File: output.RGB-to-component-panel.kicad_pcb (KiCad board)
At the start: 2 copper layers, 105 x 145 mm, 256 parts, among them J1 VGA, J3 USB_C_Receptacle_Power, J4 SCART_CONN, J5 3xRCA_CONN, U1 SC6206B-65K5, U101 TPF144-VR, U2 TPF144-VR, U3 RS8752XM, U6 74AHCT1G86, U7 74AHCT1G86, U8 LM1881

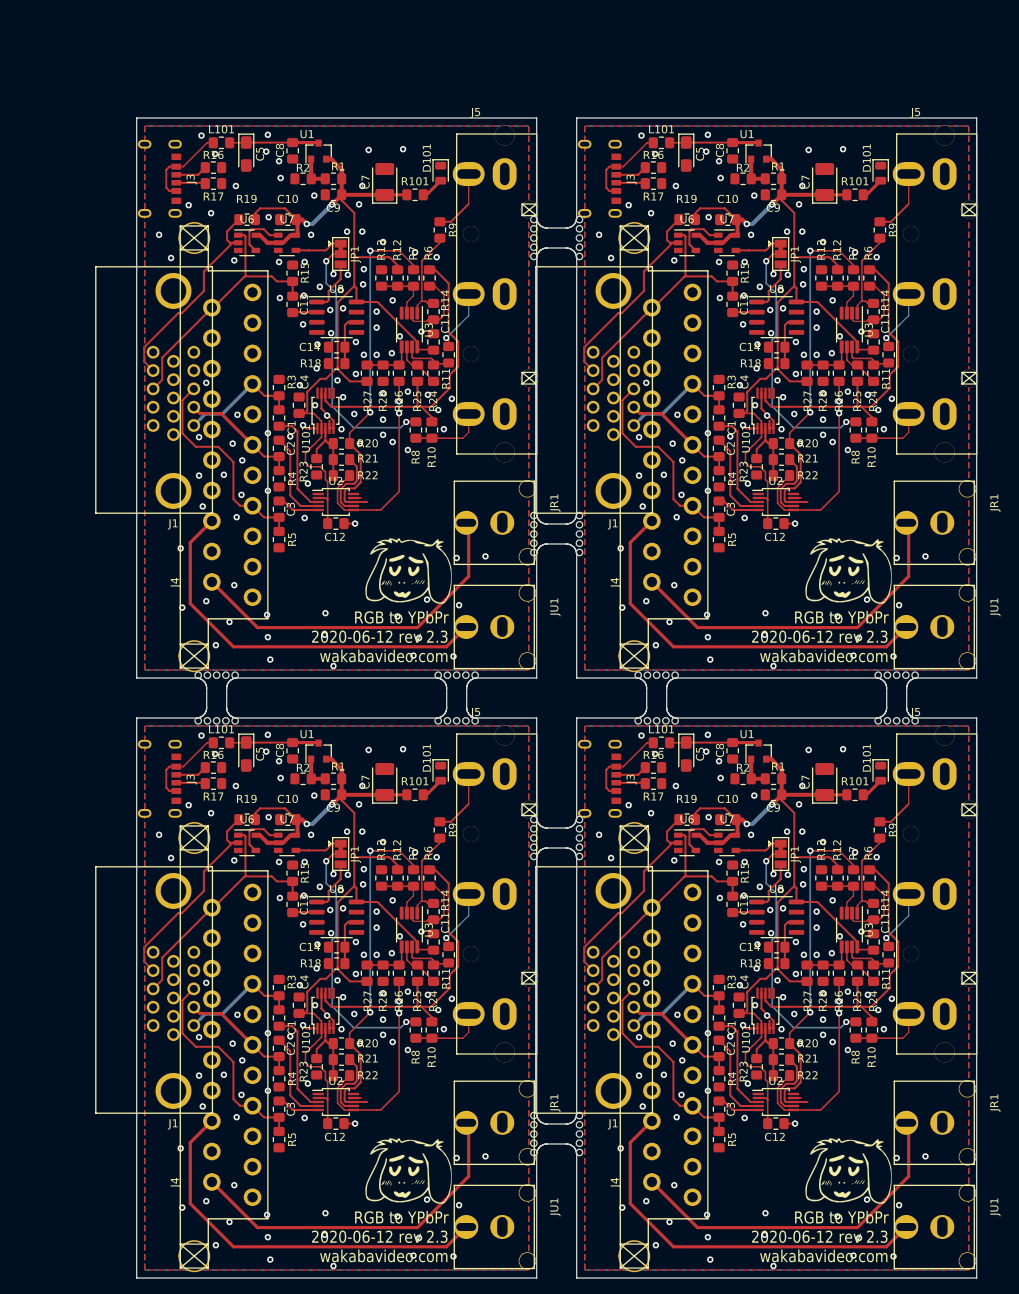
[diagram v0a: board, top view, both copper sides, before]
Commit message: swapped opamp for SOIC package
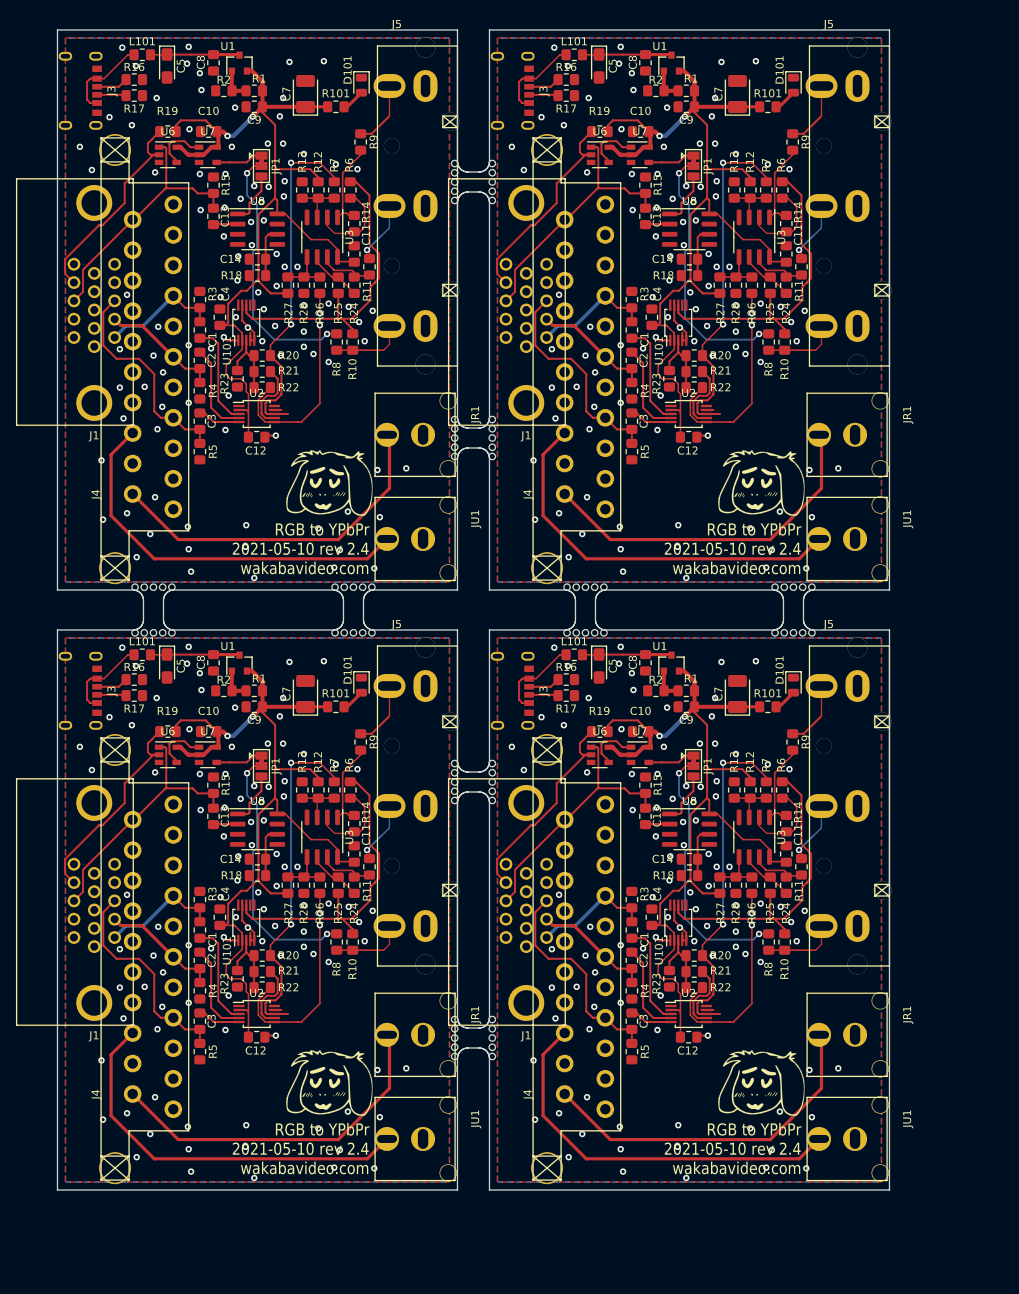
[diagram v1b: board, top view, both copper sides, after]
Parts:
- removed the ? at (79.5, 180.3)
- removed the ? at (122.5, 120.7)
- removed the ? at (97.1, 126.3)
- removed the ? at (92.5, 120.7)
- removed the ? at (67.5, 120.7)
- removed the ? at (72.1, 126.3)
- removed the ? at (37.5, 120.7)
- removed the ? at (42.1, 126.3)
- removed the ? at (85.2, 175.7)
- removed the ? at (79.5, 143.3)
- removed the ? at (85.2, 138.7)
- removed the ? at (79.5, 105.3)
- removed the ? at (85.2, 100.7)
- removed the ? at (79.5, 68.3)
- removed the ? at (85.2, 63.7)
- removed the ? at (127.1, 126.3)
- removed the C1 at (102.6, 163.5)
- removed the C1 at (47.6, 163.5)
- removed the C1 at (47.6, 88.5)
- removed the C1 at (102.6, 88.5)
- removed the C10 at (103.7, 138.7)
- removed the C10 at (48.7, 138.7)
- removed the C10 at (48.7, 63.7)
- removed the C10 at (103.7, 63.7)
- removed the C11 at (121.9, 154.0)
- removed the C11 at (66.9, 154.0)
- removed the C11 at (66.9, 79.0)
- removed the C11 at (121.9, 79.0)
- removed the C12 at (109.7, 176.7)
- removed the C12 at (54.7, 176.7)
- removed the C12 at (54.7, 101.7)
- removed the C12 at (109.7, 101.7)
- removed the C13 at (104.3, 149.3)
- removed the C13 at (49.3, 149.3)
- removed the C13 at (49.3, 74.3)
- removed the C13 at (104.3, 74.3)
- removed the C14 at (109.8, 154.7)
- removed the C14 at (54.8, 154.7)
- removed the C14 at (54.8, 79.7)
- removed the C14 at (109.8, 79.7)
- removed the C2 at (102.6, 167.3)
- removed the C2 at (47.6, 167.3)
- removed the C2 at (47.6, 92.3)
- removed the C2 at (102.6, 92.3)
- removed the C3 at (102.6, 174.9)
- removed the C3 at (47.6, 174.9)
- removed the C3 at (47.6, 99.9)
- removed the C3 at (102.6, 99.9)
- removed the C4 at (105.1, 161.9)
- removed the C4 at (50.1, 161.9)
- removed the C4 at (50.1, 86.9)
- removed the C4 at (105.1, 86.9)
- removed the C5 at (98.5, 130.5)
- removed the C5 at (43.5, 130.5)
- removed the C5 at (43.5, 55.5)
- removed the C5 at (98.5, 55.5)
- removed the C7 at (115.8, 134.0)
- removed the C7 at (60.8, 134.0)
- removed the C7 at (60.8, 59.0)
- removed the C7 at (115.8, 59.0)
- removed the C8 at (104.3, 130.1)
- removed the C8 at (49.3, 130.1)
- removed the C8 at (49.3, 55.1)
- removed the C8 at (104.3, 55.1)
- removed the C9 at (109.4, 135.6)
- removed the C9 at (54.4, 135.6)
- removed the C9 at (54.4, 60.6)
- removed the C9 at (109.4, 60.6)
- removed the D101 at (122.8, 132.9)
- removed the D101 at (67.8, 132.9)
- removed the D101 at (67.8, 57.9)
- removed the D101 at (122.8, 57.9)
- removed the GOTE1 at (118.8, 182.6)
- removed the GOTE1 at (63.8, 182.6)
- removed the GOTE1 at (63.8, 107.6)
- removed the GOTE1 at (118.8, 107.6)
- removed the GOTE2 at (112.6, 166.7)
- removed the GOTE2 at (57.6, 166.7)
- removed the GOTE2 at (57.6, 91.7)
- removed the GOTE2 at (112.6, 91.7)
- removed the J1 at (89.4, 161.0)
- removed the J1 at (34.4, 161.0)
- removed the J1 at (34.4, 86.0)
- removed the J1 at (89.4, 86.0)
- removed the J3 at (83.2, 133.6)
- removed the J3 at (28.2, 133.6)
- removed the J3 at (28.2, 58.6)
- removed the J3 at (83.2, 58.6)
- removed the J4 at (94.2, 184.0)
- removed the J4 at (39.2, 184.0)
- removed the J4 at (39.2, 109.0)
- removed the J4 at (94.2, 109.0)
- removed the J5 at (130.8, 148.0)
- removed the J5 at (75.8, 148.0)
- removed the J5 at (75.8, 73.0)
- removed the J5 at (130.8, 73.0)
- removed the JP1 at (110.3, 143.0)
- removed the JP1 at (55.3, 143.0)
- removed the JP1 at (55.3, 68.0)
- removed the JP1 at (110.3, 68.0)
- removed the JR1 at (134.5, 176.6)
- removed the JR1 at (79.5, 176.6)
- removed the JR1 at (79.5, 101.6)
- removed the JR1 at (134.5, 101.6)
- removed the JU1 at (134.5, 189.6)
- removed the JU1 at (79.5, 189.6)
- removed the JU1 at (79.5, 114.6)
- removed the JU1 at (134.5, 114.6)
- removed the L101 at (95.4, 129.1)
- removed the L101 at (40.4, 129.1)
- removed the L101 at (40.4, 54.1)
- removed the L101 at (95.4, 54.1)
- removed the R1 at (109.4, 133.6)
- removed the R1 at (54.4, 133.6)
- removed the R1 at (54.4, 58.6)
- removed the R1 at (109.4, 58.6)
- removed the R10 at (121.7, 165.0)
- removed the R10 at (66.7, 165.0)
- removed the R10 at (66.7, 90.0)
- removed the R10 at (121.7, 90.0)
- removed the R101 at (119.6, 135.6)
- removed the R101 at (64.6, 135.6)
- removed the R101 at (64.6, 60.6)
- removed the R101 at (119.6, 60.6)
- removed the R11 at (123.8, 155.6)
- removed the R11 at (68.8, 155.6)
- removed the R11 at (68.8, 80.6)
- removed the R11 at (123.8, 80.6)
- removed the R12 at (117.4, 146.0)
- removed the R12 at (62.4, 146.0)
- removed the R12 at (62.4, 71.0)
- removed the R12 at (117.4, 71.0)
- removed the R13 at (115.4, 146.0)
- removed the R13 at (60.4, 146.0)
- removed the R13 at (60.4, 71.0)
- removed the R13 at (115.4, 71.0)
- removed the R14 at (121.9, 150.2)
- removed the R14 at (66.9, 150.2)
- removed the R14 at (66.9, 75.2)
- removed the R14 at (121.9, 75.2)
- removed the R15 at (104.3, 145.4)
- removed the R15 at (49.3, 145.4)
- removed the R15 at (49.3, 70.4)
- removed the R15 at (104.3, 70.4)
- removed the R16 at (94.4, 132.2)
- removed the R16 at (39.4, 132.2)
- removed the R16 at (39.4, 57.2)
- removed the R16 at (94.4, 57.2)
- removed the R17 at (94.4, 134.2)
- removed the R17 at (39.4, 134.2)
- removed the R17 at (39.4, 59.2)
- removed the R17 at (94.4, 59.2)
- removed the R18 at (109.8, 156.7)
- removed the R18 at (54.8, 156.7)
- removed the R18 at (54.8, 81.7)
- removed the R18 at (109.8, 81.7)
- removed the R19 at (98.6, 138.7)
- removed the R19 at (43.6, 138.7)
- removed the R19 at (43.6, 63.7)
- removed the R19 at (98.6, 63.7)
- removed the R2 at (105.6, 133.6)
- removed the R2 at (50.6, 133.6)
- removed the R2 at (50.6, 58.6)
- removed the R2 at (105.6, 58.6)
- removed the R20 at (110.4, 166.7)
- removed the R20 at (55.4, 166.7)
- removed the R20 at (55.4, 91.7)
- removed the R20 at (110.4, 91.7)
- removed the R21 at (110.4, 168.7)
- removed the R21 at (55.4, 168.7)
- removed the R21 at (55.4, 93.7)
- removed the R21 at (110.4, 93.7)
- removed the R22 at (110.4, 170.7)
- removed the R22 at (55.4, 170.7)
- removed the R22 at (55.4, 95.7)
- removed the R22 at (110.4, 95.7)
- removed the R23 at (107.3, 169.6)
- removed the R23 at (52.3, 169.6)
- removed the R23 at (52.3, 94.6)
- removed the R23 at (107.3, 94.6)
- removed the R24 at (121.9, 157.9)
- removed the R24 at (66.9, 157.9)
- removed the R24 at (66.9, 82.9)
- removed the R24 at (121.9, 82.9)
- removed the R25 at (119.9, 157.9)
- removed the R25 at (64.9, 157.9)
- removed the R25 at (64.9, 82.9)
- removed the R25 at (119.9, 82.9)
- removed the R26 at (117.6, 157.9)
- removed the R26 at (62.6, 157.9)
- removed the R26 at (62.6, 82.9)
- removed the R26 at (117.6, 82.9)
- removed the R27 at (113.6, 157.9)
- removed the R27 at (58.6, 157.9)
- removed the R27 at (58.6, 82.9)
- removed the R27 at (113.6, 82.9)
- removed the R28 at (115.6, 157.9)
- removed the R28 at (60.6, 157.9)
- removed the R28 at (60.6, 82.9)
- removed the R28 at (115.6, 82.9)
- removed the R3 at (102.6, 159.7)
- removed the R3 at (47.6, 159.7)
- removed the R3 at (47.6, 84.7)
- removed the R3 at (102.6, 84.7)
- removed the R4 at (102.6, 171.1)
- removed the R4 at (47.6, 171.1)
- removed the R4 at (47.6, 96.1)
- removed the R4 at (102.6, 96.1)
- removed the R5 at (102.6, 178.7)
- removed the R5 at (47.6, 178.7)
- removed the R5 at (47.6, 103.7)
- removed the R5 at (102.6, 103.7)
- removed the R6 at (121.4, 146.0)
- removed the R6 at (66.4, 146.0)
- removed the R6 at (66.4, 71.0)
- removed the R6 at (121.4, 71.0)
- removed the R7 at (119.4, 146.0)
- removed the R7 at (64.4, 146.0)
- removed the R7 at (64.4, 71.0)
- removed the R7 at (119.4, 71.0)
- removed the R8 at (119.7, 165.0)
- removed the R8 at (64.7, 165.0)
- removed the R8 at (64.7, 90.0)
- removed the R8 at (119.7, 90.0)
- removed the R9 at (122.7, 140.0)
- removed the R9 at (67.7, 140.0)
- removed the R9 at (67.7, 65.0)
- removed the R9 at (122.7, 65.0)
- removed the U1 at (107.5, 130.1)
- removed the U1 at (52.5, 130.1)
- removed the U1 at (52.5, 55.1)
- removed the U1 at (107.5, 55.1)
- removed the U101 at (108.4, 162.6)
- removed the U101 at (53.4, 162.6)
- removed the U101 at (53.4, 87.6)
- removed the U101 at (108.4, 87.6)
- removed the U2 at (109.7, 174.0)
- removed the U2 at (54.7, 174.0)
- removed the U2 at (54.7, 99.0)
- removed the U2 at (109.7, 99.0)
- removed the U3 at (118.9, 152.5)
- removed the U3 at (63.9, 152.5)
- removed the U3 at (63.9, 77.5)
- removed the U3 at (118.9, 77.5)
- removed the U6 at (98.6, 141.6)
- removed the U6 at (43.6, 141.6)
- removed the U6 at (43.6, 66.6)
- removed the U6 at (98.6, 66.6)
- removed the U7 at (103.6, 141.6)
- removed the U7 at (48.6, 141.6)
- removed the U7 at (48.6, 66.6)
- removed the U7 at (103.6, 66.6)
- removed the U8 at (109.8, 150.9)
- removed the U8 at (54.8, 150.9)
- removed the U8 at (54.8, 75.9)
- removed the U8 at (109.8, 75.9)
- added ?: , holes, F.Cu at (109.6, 109.6)
- added ?: , holes, F.Cu at (74.2, 131.7)
- added ?: , holes, F.Cu at (69.5, 168.3)
- added ?: , holes, F.Cu at (74.2, 163.7)
- added ?: , holes, F.Cu at (69.6, 61.3)
- added ?: , holes, F.Cu at (74.2, 56.7)
- added ?: , holes, F.Cu at (69.5, 93.3)
- added ?: , holes, F.Cu at (74.2, 88.7)
- added ?: , holes, F.Cu at (114.2, 115.4)
- added ?: , holes, F.Cu at (83.6, 109.7)
- added ?: , holes, F.Cu at (88.2, 115.3)
- added ?: , holes, F.Cu at (54.6, 109.7)
- added ?: , holes, F.Cu at (59.2, 115.3)
- added ?: , holes, F.Cu at (29.6, 109.7)
- added ?: , holes, F.Cu at (34.2, 115.3)
- added ?: , holes, F.Cu at (69.6, 136.3)
- added C1: 1u, Capacitor_SMD:C_0805_2012Metric_Pad1.15x1.40mm_HandSolder, F.Cu at (37.7, 152.5)
- added C1: 1u, Capacitor_SMD:C_0805_2012Metric_Pad1.15x1.40mm_HandSolder, F.Cu at (91.7, 152.5)
- added C1: 1u, Capacitor_SMD:C_0805_2012Metric_Pad1.15x1.40mm_HandSolder, F.Cu at (91.7, 77.5)
- added C1: 1u, Capacitor_SMD:C_0805_2012Metric_Pad1.15x1.40mm_HandSolder, F.Cu at (37.7, 77.5)
- added C10: 100n, Capacitor_SMD:C_0805_2012Metric_Pad1.15x1.40mm_HandSolder, F.Cu at (92.8, 127.7)
- added C10: 100n, Capacitor_SMD:C_0805_2012Metric_Pad1.15x1.40mm_HandSolder, F.Cu at (38.8, 127.7)
- added C10: 100n, Capacitor_SMD:C_0805_2012Metric_Pad1.15x1.40mm_HandSolder, F.Cu at (92.8, 52.7)
- added C10: 100n, Capacitor_SMD:C_0805_2012Metric_Pad1.15x1.40mm_HandSolder, F.Cu at (38.8, 52.7)
- added C11: 100n, Capacitor_SMD:C_0805_2012Metric_Pad1.15x1.40mm_HandSolder, F.Cu at (111.0, 143.0)
- added C11: 100n, Capacitor_SMD:C_0805_2012Metric_Pad1.15x1.40mm_HandSolder, F.Cu at (57.0, 143.0)
- added C11: 100n, Capacitor_SMD:C_0805_2012Metric_Pad1.15x1.40mm_HandSolder, F.Cu at (111.0, 68.0)
- added C11: 100n, Capacitor_SMD:C_0805_2012Metric_Pad1.15x1.40mm_HandSolder, F.Cu at (57.0, 68.0)
- added C12: 100n, Capacitor_SMD:C_0805_2012Metric_Pad1.15x1.40mm_HandSolder, F.Cu at (44.8, 165.9)
- added C12: 100n, Capacitor_SMD:C_0805_2012Metric_Pad1.15x1.40mm_HandSolder, F.Cu at (98.8, 165.9)
- added C12: 100n, Capacitor_SMD:C_0805_2012Metric_Pad1.15x1.40mm_HandSolder, F.Cu at (98.8, 90.9)
- added C12: 100n, Capacitor_SMD:C_0805_2012Metric_Pad1.15x1.40mm_HandSolder, F.Cu at (44.8, 90.9)
- added C13: 100n, Capacitor_SMD:C_0805_2012Metric_Pad1.15x1.40mm_HandSolder, F.Cu at (93.4, 138.3)
- added C13: 100n, Capacitor_SMD:C_0805_2012Metric_Pad1.15x1.40mm_HandSolder, F.Cu at (39.4, 138.3)
- added C13: 100n, Capacitor_SMD:C_0805_2012Metric_Pad1.15x1.40mm_HandSolder, F.Cu at (93.4, 63.3)
- added C13: 100n, Capacitor_SMD:C_0805_2012Metric_Pad1.15x1.40mm_HandSolder, F.Cu at (39.4, 63.3)
- added C14: 100n, Capacitor_SMD:C_0805_2012Metric_Pad1.15x1.40mm_HandSolder, F.Cu at (98.9, 143.7)
- added C14: 100n, Capacitor_SMD:C_0805_2012Metric_Pad1.15x1.40mm_HandSolder, F.Cu at (44.9, 143.7)
- added C14: 100n, Capacitor_SMD:C_0805_2012Metric_Pad1.15x1.40mm_HandSolder, F.Cu at (98.9, 68.7)
- added C14: 100n, Capacitor_SMD:C_0805_2012Metric_Pad1.15x1.40mm_HandSolder, F.Cu at (44.9, 68.7)
- added C2: 1u, Capacitor_SMD:C_0805_2012Metric_Pad1.15x1.40mm_HandSolder, F.Cu at (37.7, 156.3)
- added C2: 1u, Capacitor_SMD:C_0805_2012Metric_Pad1.15x1.40mm_HandSolder, F.Cu at (91.7, 156.3)
- added C2: 1u, Capacitor_SMD:C_0805_2012Metric_Pad1.15x1.40mm_HandSolder, F.Cu at (91.7, 81.3)
- added C2: 1u, Capacitor_SMD:C_0805_2012Metric_Pad1.15x1.40mm_HandSolder, F.Cu at (37.7, 81.3)
- added C3: 1u, Capacitor_SMD:C_0805_2012Metric_Pad1.15x1.40mm_HandSolder, F.Cu at (37.7, 163.9)
- added C3: 1u, Capacitor_SMD:C_0805_2012Metric_Pad1.15x1.40mm_HandSolder, F.Cu at (91.7, 163.9)
- added C3: 1u, Capacitor_SMD:C_0805_2012Metric_Pad1.15x1.40mm_HandSolder, F.Cu at (91.7, 88.9)
- added C3: 1u, Capacitor_SMD:C_0805_2012Metric_Pad1.15x1.40mm_HandSolder, F.Cu at (37.7, 88.9)
- added C4: 100n, Capacitor_SMD:C_0805_2012Metric_Pad1.15x1.40mm_HandSolder, F.Cu at (94.2, 150.9)
- added C4: 100n, Capacitor_SMD:C_0805_2012Metric_Pad1.15x1.40mm_HandSolder, F.Cu at (40.2, 150.9)
- added C4: 100n, Capacitor_SMD:C_0805_2012Metric_Pad1.15x1.40mm_HandSolder, F.Cu at (94.2, 75.9)
- added C4: 100n, Capacitor_SMD:C_0805_2012Metric_Pad1.15x1.40mm_HandSolder, F.Cu at (40.2, 75.9)
- added C5: 10u, Capacitor_Tantalum_SMD:CP_EIA-3216-18_Kemet-A_Pad1.58x1.35mm_HandSolder, F.Cu at (33.6, 119.5)
- added C5: 10u, Capacitor_Tantalum_SMD:CP_EIA-3216-18_Kemet-A_Pad1.58x1.35mm_HandSolder, F.Cu at (87.6, 119.5)
- added C5: 10u, Capacitor_Tantalum_SMD:CP_EIA-3216-18_Kemet-A_Pad1.58x1.35mm_HandSolder, F.Cu at (87.6, 44.5)
- added C5: 10u, Capacitor_Tantalum_SMD:CP_EIA-3216-18_Kemet-A_Pad1.58x1.35mm_HandSolder, F.Cu at (33.6, 44.5)
- added C7: 100u, Capacitor_Tantalum_SMD:CP_EIA-3528-21_Kemet-B_Pad1.50x2.35mm_HandSolder, F.Cu at (50.9, 123.0)
- added C7: 100u, Capacitor_Tantalum_SMD:CP_EIA-3528-21_Kemet-B_Pad1.50x2.35mm_HandSolder, F.Cu at (104.9, 123.0)
- added C7: 100u, Capacitor_Tantalum_SMD:CP_EIA-3528-21_Kemet-B_Pad1.50x2.35mm_HandSolder, F.Cu at (104.9, 48.0)
- added C7: 100u, Capacitor_Tantalum_SMD:CP_EIA-3528-21_Kemet-B_Pad1.50x2.35mm_HandSolder, F.Cu at (50.9, 48.0)
- added C8: 100n, Capacitor_SMD:C_0805_2012Metric_Pad1.15x1.40mm_HandSolder, F.Cu at (39.4, 119.1)
- added C8: 100n, Capacitor_SMD:C_0805_2012Metric_Pad1.15x1.40mm_HandSolder, F.Cu at (93.4, 119.1)
- added C8: 100n, Capacitor_SMD:C_0805_2012Metric_Pad1.15x1.40mm_HandSolder, F.Cu at (93.4, 44.1)
- added C8: 100n, Capacitor_SMD:C_0805_2012Metric_Pad1.15x1.40mm_HandSolder, F.Cu at (39.4, 44.1)
- added C9: 10u, Capacitor_SMD:C_0805_2012Metric_Pad1.15x1.40mm_HandSolder, F.Cu at (44.5, 124.6)
- added C9: 10u, Capacitor_SMD:C_0805_2012Metric_Pad1.15x1.40mm_HandSolder, F.Cu at (98.5, 124.6)
- added C9: 10u, Capacitor_SMD:C_0805_2012Metric_Pad1.15x1.40mm_HandSolder, F.Cu at (98.5, 49.6)
- added C9: 10u, Capacitor_SMD:C_0805_2012Metric_Pad1.15x1.40mm_HandSolder, F.Cu at (44.5, 49.6)
- added D101: LED, LED_SMD:LED_0805_2012Metric, F.Cu at (57.9, 121.9)
- added D101: LED, LED_SMD:LED_0805_2012Metric, F.Cu at (111.9, 121.9)
- added D101: LED, LED_SMD:LED_0805_2012Metric, F.Cu at (111.9, 46.9)
- added D101: LED, LED_SMD:LED_0805_2012Metric, F.Cu at (57.9, 46.9)
- added GOTE1: Fiducial, videobits:uwuriel, F.Cu at (107.9, 171.6)
- added GOTE1: Fiducial, videobits:uwuriel, F.Cu at (53.9, 171.6)
- added GOTE1: Fiducial, videobits:uwuriel, F.Cu at (107.9, 96.6)
- added GOTE1: Fiducial, videobits:uwuriel, F.Cu at (53.9, 96.6)
- added GOTE2: Fiducial, videobits:borgar, B.Cu at (47.7, 155.7)
- added GOTE2: Fiducial, videobits:borgar, B.Cu at (101.7, 155.7)
- added GOTE2: Fiducial, videobits:borgar, B.Cu at (101.7, 80.7)
- added GOTE2: Fiducial, videobits:borgar, B.Cu at (47.7, 80.7)
- added J1: VGA, custom_components:VGA_CONN, F.Cu at (24.5, 150.0)
- added J1: VGA, custom_components:VGA_CONN, F.Cu at (78.5, 150.0)
- added J1: VGA, custom_components:VGA_CONN, F.Cu at (78.5, 75.0)
- added J1: VGA, custom_components:VGA_CONN, F.Cu at (24.5, 75.0)
- added J3: USB_C_Receptacle_Power, videobits:USB_C_Receptacle_Generic_Power_Only, F.Cu at (72.3, 122.6)
- added J3: USB_C_Receptacle_Power, videobits:USB_C_Receptacle_Generic_Power_Only, F.Cu at (18.3, 122.6)
- added J3: USB_C_Receptacle_Power, videobits:USB_C_Receptacle_Generic_Power_Only, F.Cu at (72.3, 47.6)
- added J3: USB_C_Receptacle_Power, videobits:USB_C_Receptacle_Generic_Power_Only, F.Cu at (18.3, 47.6)
- added J4: SCART_CONN, custom_components:SCART_CONN, F.Cu at (83.3, 173.0)
- added J4: SCART_CONN, custom_components:SCART_CONN, F.Cu at (29.3, 173.0)
- added J4: SCART_CONN, custom_components:SCART_CONN, F.Cu at (83.3, 98.0)
- added J4: SCART_CONN, custom_components:SCART_CONN, F.Cu at (29.3, 98.0)
- added J5: 3xRCA_CONN, videobits:3xRCA_CONN_SINGLE, F.Cu at (65.9, 137.0)
- added J5: 3xRCA_CONN, videobits:3xRCA_CONN_SINGLE, F.Cu at (119.9, 137.0)
- added J5: 3xRCA_CONN, videobits:3xRCA_CONN_SINGLE, F.Cu at (119.9, 62.0)
- added J5: 3xRCA_CONN, videobits:3xRCA_CONN_SINGLE, F.Cu at (65.9, 62.0)
- added JP1: Jumper_3_Bridged12, Jumper:SolderJumper-3_P1.3mm_Bridged12_Pad1.0x1.5mm, F.Cu at (99.4, 132.0)
- added JP1: Jumper_3_Bridged12, Jumper:SolderJumper-3_P1.3mm_Bridged12_Pad1.0x1.5mm, F.Cu at (45.4, 132.0)
- added JP1: Jumper_3_Bridged12, Jumper:SolderJumper-3_P1.3mm_Bridged12_Pad1.0x1.5mm, F.Cu at (99.4, 57.0)
- added JP1: Jumper_3_Bridged12, Jumper:SolderJumper-3_P1.3mm_Bridged12_Pad1.0x1.5mm, F.Cu at (45.4, 57.0)
- added JR1: Conn_Coaxial, videobits:Cheapo_RCA_single_edge, F.Cu at (69.6, 165.6)
- added JR1: Conn_Coaxial, videobits:Cheapo_RCA_single_edge, F.Cu at (123.6, 165.6)
- added JR1: Conn_Coaxial, videobits:Cheapo_RCA_single_edge, F.Cu at (123.6, 90.6)
- added JR1: Conn_Coaxial, videobits:Cheapo_RCA_single_edge, F.Cu at (69.6, 90.6)
- added JU1: Conn_Coaxial, videobits:Cheapo_RCA_single_edge, F.Cu at (123.6, 178.6)
- added JU1: Conn_Coaxial, videobits:Cheapo_RCA_single_edge, F.Cu at (69.6, 178.6)
- added JU1: Conn_Coaxial, videobits:Cheapo_RCA_single_edge, F.Cu at (123.6, 103.6)
- added JU1: Conn_Coaxial, videobits:Cheapo_RCA_single_edge, F.Cu at (69.6, 103.6)
- added L101: 10u, Inductor_SMD:L_0805_2012Metric_Pad1.15x1.40mm_HandSolder, F.Cu at (30.5, 118.1)
- added L101: 10u, Inductor_SMD:L_0805_2012Metric_Pad1.15x1.40mm_HandSolder, F.Cu at (84.5, 118.1)
- added L101: 10u, Inductor_SMD:L_0805_2012Metric_Pad1.15x1.40mm_HandSolder, F.Cu at (84.5, 43.1)
- added L101: 10u, Inductor_SMD:L_0805_2012Metric_Pad1.15x1.40mm_HandSolder, F.Cu at (30.5, 43.1)
- added R1: 1k, Resistor_SMD:R_0805_2012Metric_Pad1.15x1.40mm_HandSolder, F.Cu at (44.5, 122.6)
- added R1: 1k, Resistor_SMD:R_0805_2012Metric_Pad1.15x1.40mm_HandSolder, F.Cu at (98.5, 122.6)
- added R1: 1k, Resistor_SMD:R_0805_2012Metric_Pad1.15x1.40mm_HandSolder, F.Cu at (98.5, 47.6)
- added R1: 1k, Resistor_SMD:R_0805_2012Metric_Pad1.15x1.40mm_HandSolder, F.Cu at (44.5, 47.6)
- added R10: 75, Resistor_SMD:R_0805_2012Metric_Pad1.15x1.40mm_HandSolder, F.Cu at (110.8, 154.0)
- added R10: 75, Resistor_SMD:R_0805_2012Metric_Pad1.15x1.40mm_HandSolder, F.Cu at (56.8, 154.0)
- added R10: 75, Resistor_SMD:R_0805_2012Metric_Pad1.15x1.40mm_HandSolder, F.Cu at (110.8, 79.0)
- added R10: 75, Resistor_SMD:R_0805_2012Metric_Pad1.15x1.40mm_HandSolder, F.Cu at (56.8, 79.0)
- added R101: 1k, Resistor_SMD:R_0805_2012Metric_Pad1.15x1.40mm_HandSolder, F.Cu at (54.7, 124.6)
- added R101: 1k, Resistor_SMD:R_0805_2012Metric_Pad1.15x1.40mm_HandSolder, F.Cu at (108.7, 124.6)
- added R101: 1k, Resistor_SMD:R_0805_2012Metric_Pad1.15x1.40mm_HandSolder, F.Cu at (108.7, 49.6)
- added R101: 1k, Resistor_SMD:R_0805_2012Metric_Pad1.15x1.40mm_HandSolder, F.Cu at (54.7, 49.6)
- added R11: 75, Resistor_SMD:R_0805_2012Metric_Pad1.15x1.40mm_HandSolder, F.Cu at (58.9, 144.6)
- added R11: 75, Resistor_SMD:R_0805_2012Metric_Pad1.15x1.40mm_HandSolder, F.Cu at (112.9, 144.6)
- added R11: 75, Resistor_SMD:R_0805_2012Metric_Pad1.15x1.40mm_HandSolder, F.Cu at (112.9, 69.6)
- added R11: 75, Resistor_SMD:R_0805_2012Metric_Pad1.15x1.40mm_HandSolder, F.Cu at (58.9, 69.6)
- added R12: 4k7, Resistor_SMD:R_0805_2012Metric_Pad1.15x1.40mm_HandSolder, F.Cu at (52.5, 135.0)
- added R12: 4k7, Resistor_SMD:R_0805_2012Metric_Pad1.15x1.40mm_HandSolder, F.Cu at (106.5, 135.0)
- added R12: 4k7, Resistor_SMD:R_0805_2012Metric_Pad1.15x1.40mm_HandSolder, F.Cu at (106.5, 60.0)
- added R12: 4k7, Resistor_SMD:R_0805_2012Metric_Pad1.15x1.40mm_HandSolder, F.Cu at (52.5, 60.0)
- added R13: 1k27, Resistor_SMD:R_0805_2012Metric_Pad1.15x1.40mm_HandSolder, F.Cu at (104.5, 135.0)
- added R13: 1k27, Resistor_SMD:R_0805_2012Metric_Pad1.15x1.40mm_HandSolder, F.Cu at (50.5, 135.0)
- added R13: 1k27, Resistor_SMD:R_0805_2012Metric_Pad1.15x1.40mm_HandSolder, F.Cu at (104.5, 60.0)
- added R13: 1k27, Resistor_SMD:R_0805_2012Metric_Pad1.15x1.40mm_HandSolder, F.Cu at (50.5, 60.0)
- added R14: 1k, Resistor_SMD:R_0805_2012Metric_Pad1.15x1.40mm_HandSolder, F.Cu at (111.0, 139.2)
- added R14: 1k, Resistor_SMD:R_0805_2012Metric_Pad1.15x1.40mm_HandSolder, F.Cu at (57.0, 139.2)
- added R14: 1k, Resistor_SMD:R_0805_2012Metric_Pad1.15x1.40mm_HandSolder, F.Cu at (111.0, 64.2)
- added R14: 1k, Resistor_SMD:R_0805_2012Metric_Pad1.15x1.40mm_HandSolder, F.Cu at (57.0, 64.2)
- added R15: 75, Resistor_SMD:R_0805_2012Metric_Pad1.15x1.40mm_HandSolder, F.Cu at (93.4, 134.4)
- added R15: 75, Resistor_SMD:R_0805_2012Metric_Pad1.15x1.40mm_HandSolder, F.Cu at (39.4, 134.4)
- added R15: 75, Resistor_SMD:R_0805_2012Metric_Pad1.15x1.40mm_HandSolder, F.Cu at (93.4, 59.4)
- added R15: 75, Resistor_SMD:R_0805_2012Metric_Pad1.15x1.40mm_HandSolder, F.Cu at (39.4, 59.4)
- added R16: 5k1, Resistor_SMD:R_0805_2012Metric_Pad1.15x1.40mm_HandSolder, F.Cu at (83.5, 121.2)
- added R16: 5k1, Resistor_SMD:R_0805_2012Metric_Pad1.15x1.40mm_HandSolder, F.Cu at (29.5, 121.2)
- added R16: 5k1, Resistor_SMD:R_0805_2012Metric_Pad1.15x1.40mm_HandSolder, F.Cu at (83.5, 46.2)
- added R16: 5k1, Resistor_SMD:R_0805_2012Metric_Pad1.15x1.40mm_HandSolder, F.Cu at (29.5, 46.2)
- added R17: 5k1, Resistor_SMD:R_0805_2012Metric_Pad1.15x1.40mm_HandSolder, F.Cu at (83.5, 123.2)
- added R17: 5k1, Resistor_SMD:R_0805_2012Metric_Pad1.15x1.40mm_HandSolder, F.Cu at (29.5, 123.2)
- added R17: 5k1, Resistor_SMD:R_0805_2012Metric_Pad1.15x1.40mm_HandSolder, F.Cu at (83.5, 48.2)
- added R17: 5k1, Resistor_SMD:R_0805_2012Metric_Pad1.15x1.40mm_HandSolder, F.Cu at (29.5, 48.2)
- added R18: 680k, Resistor_SMD:R_0805_2012Metric_Pad1.15x1.40mm_HandSolder, F.Cu at (98.9, 145.7)
- added R18: 680k, Resistor_SMD:R_0805_2012Metric_Pad1.15x1.40mm_HandSolder, F.Cu at (44.9, 145.7)
- added R18: 680k, Resistor_SMD:R_0805_2012Metric_Pad1.15x1.40mm_HandSolder, F.Cu at (98.9, 70.7)
- added R18: 680k, Resistor_SMD:R_0805_2012Metric_Pad1.15x1.40mm_HandSolder, F.Cu at (44.9, 70.7)
- added R19: 1k, Resistor_SMD:R_0805_2012Metric_Pad1.15x1.40mm_HandSolder, F.Cu at (87.7, 127.7)
- added R19: 1k, Resistor_SMD:R_0805_2012Metric_Pad1.15x1.40mm_HandSolder, F.Cu at (33.7, 127.7)
- added R19: 1k, Resistor_SMD:R_0805_2012Metric_Pad1.15x1.40mm_HandSolder, F.Cu at (87.7, 52.7)
- added R19: 1k, Resistor_SMD:R_0805_2012Metric_Pad1.15x1.40mm_HandSolder, F.Cu at (33.7, 52.7)
- added R2: 1k33, Resistor_SMD:R_0805_2012Metric_Pad1.15x1.40mm_HandSolder, F.Cu at (40.7, 122.6)
- added R2: 1k33, Resistor_SMD:R_0805_2012Metric_Pad1.15x1.40mm_HandSolder, F.Cu at (94.7, 122.6)
- added R2: 1k33, Resistor_SMD:R_0805_2012Metric_Pad1.15x1.40mm_HandSolder, F.Cu at (94.7, 47.6)
- added R2: 1k33, Resistor_SMD:R_0805_2012Metric_Pad1.15x1.40mm_HandSolder, F.Cu at (40.7, 47.6)
- added R20: 1k, Resistor_SMD:R_0805_2012Metric_Pad1.15x1.40mm_HandSolder, F.Cu at (45.5, 155.7)
- added R20: 1k, Resistor_SMD:R_0805_2012Metric_Pad1.15x1.40mm_HandSolder, F.Cu at (99.5, 155.7)
- added R20: 1k, Resistor_SMD:R_0805_2012Metric_Pad1.15x1.40mm_HandSolder, F.Cu at (99.5, 80.7)
- added R20: 1k, Resistor_SMD:R_0805_2012Metric_Pad1.15x1.40mm_HandSolder, F.Cu at (45.5, 80.7)
- added R21: 511, Resistor_SMD:R_0805_2012Metric_Pad1.15x1.40mm_HandSolder, F.Cu at (45.5, 157.7)
- added R21: 511, Resistor_SMD:R_0805_2012Metric_Pad1.15x1.40mm_HandSolder, F.Cu at (99.5, 157.7)
- added R21: 511, Resistor_SMD:R_0805_2012Metric_Pad1.15x1.40mm_HandSolder, F.Cu at (99.5, 82.7)
- added R21: 511, Resistor_SMD:R_0805_2012Metric_Pad1.15x1.40mm_HandSolder, F.Cu at (45.5, 82.7)
- added R22: 2740, Resistor_SMD:R_0805_2012Metric_Pad1.15x1.40mm_HandSolder, F.Cu at (99.5, 159.7)
- added R22: 2740, Resistor_SMD:R_0805_2012Metric_Pad1.15x1.40mm_HandSolder, F.Cu at (45.5, 159.7)
- added R22: 2740, Resistor_SMD:R_0805_2012Metric_Pad1.15x1.40mm_HandSolder, F.Cu at (99.5, 84.7)
- added R22: 2740, Resistor_SMD:R_0805_2012Metric_Pad1.15x1.40mm_HandSolder, F.Cu at (45.5, 84.7)
- added R23: 300, Resistor_SMD:R_0805_2012Metric_Pad1.15x1.40mm_HandSolder, F.Cu at (42.4, 158.6)
- added R23: 300, Resistor_SMD:R_0805_2012Metric_Pad1.15x1.40mm_HandSolder, F.Cu at (96.4, 158.6)
- added R23: 300, Resistor_SMD:R_0805_2012Metric_Pad1.15x1.40mm_HandSolder, F.Cu at (96.4, 83.6)
- added R23: 300, Resistor_SMD:R_0805_2012Metric_Pad1.15x1.40mm_HandSolder, F.Cu at (42.4, 83.6)
- added R24: 1k, Resistor_SMD:R_0805_2012Metric_Pad1.15x1.40mm_HandSolder, F.Cu at (111.0, 146.9)
- added R24: 1k, Resistor_SMD:R_0805_2012Metric_Pad1.15x1.40mm_HandSolder, F.Cu at (57.0, 146.9)
- added R24: 1k, Resistor_SMD:R_0805_2012Metric_Pad1.15x1.40mm_HandSolder, F.Cu at (111.0, 71.9)
- added R24: 1k, Resistor_SMD:R_0805_2012Metric_Pad1.15x1.40mm_HandSolder, F.Cu at (57.0, 71.9)
- added R25: 1k77, Resistor_SMD:R_0805_2012Metric_Pad1.15x1.40mm_HandSolder, F.Cu at (55.0, 146.9)
- added R25: 1k77, Resistor_SMD:R_0805_2012Metric_Pad1.15x1.40mm_HandSolder, F.Cu at (109.0, 146.9)
- added R25: 1k77, Resistor_SMD:R_0805_2012Metric_Pad1.15x1.40mm_HandSolder, F.Cu at (109.0, 71.9)
- added R25: 1k77, Resistor_SMD:R_0805_2012Metric_Pad1.15x1.40mm_HandSolder, F.Cu at (55.0, 71.9)
- added R26: 1k77, Resistor_SMD:R_0805_2012Metric_Pad1.15x1.40mm_HandSolder, F.Cu at (106.7, 146.9)
- added R26: 1k77, Resistor_SMD:R_0805_2012Metric_Pad1.15x1.40mm_HandSolder, F.Cu at (52.7, 146.9)
- added R26: 1k77, Resistor_SMD:R_0805_2012Metric_Pad1.15x1.40mm_HandSolder, F.Cu at (106.7, 71.9)
- added R26: 1k77, Resistor_SMD:R_0805_2012Metric_Pad1.15x1.40mm_HandSolder, F.Cu at (52.7, 71.9)
- added R27: 4k7, Resistor_SMD:R_0805_2012Metric_Pad1.15x1.40mm_HandSolder, F.Cu at (102.7, 146.9)
- added R27: 4k7, Resistor_SMD:R_0805_2012Metric_Pad1.15x1.40mm_HandSolder, F.Cu at (48.7, 146.9)
- added R27: 4k7, Resistor_SMD:R_0805_2012Metric_Pad1.15x1.40mm_HandSolder, F.Cu at (102.7, 71.9)
- added R27: 4k7, Resistor_SMD:R_0805_2012Metric_Pad1.15x1.40mm_HandSolder, F.Cu at (48.7, 71.9)
- added R28: 1k27, Resistor_SMD:R_0805_2012Metric_Pad1.15x1.40mm_HandSolder, F.Cu at (104.7, 146.9)
- added R28: 1k27, Resistor_SMD:R_0805_2012Metric_Pad1.15x1.40mm_HandSolder, F.Cu at (50.7, 146.9)
- added R28: 1k27, Resistor_SMD:R_0805_2012Metric_Pad1.15x1.40mm_HandSolder, F.Cu at (104.7, 71.9)
- added R28: 1k27, Resistor_SMD:R_0805_2012Metric_Pad1.15x1.40mm_HandSolder, F.Cu at (50.7, 71.9)
- added R3: 75, Resistor_SMD:R_0805_2012Metric_Pad1.15x1.40mm_HandSolder, F.Cu at (91.7, 148.7)
- added R3: 75, Resistor_SMD:R_0805_2012Metric_Pad1.15x1.40mm_HandSolder, F.Cu at (37.7, 148.7)
- added R3: 75, Resistor_SMD:R_0805_2012Metric_Pad1.15x1.40mm_HandSolder, F.Cu at (91.7, 73.7)
- added R3: 75, Resistor_SMD:R_0805_2012Metric_Pad1.15x1.40mm_HandSolder, F.Cu at (37.7, 73.7)
- added R4: 75, Resistor_SMD:R_0805_2012Metric_Pad1.15x1.40mm_HandSolder, F.Cu at (37.7, 160.1)
- added R4: 75, Resistor_SMD:R_0805_2012Metric_Pad1.15x1.40mm_HandSolder, F.Cu at (91.7, 160.1)
- added R4: 75, Resistor_SMD:R_0805_2012Metric_Pad1.15x1.40mm_HandSolder, F.Cu at (91.7, 85.1)
- added R4: 75, Resistor_SMD:R_0805_2012Metric_Pad1.15x1.40mm_HandSolder, F.Cu at (37.7, 85.1)
- added R5: 75, Resistor_SMD:R_0805_2012Metric_Pad1.15x1.40mm_HandSolder, F.Cu at (37.7, 167.7)
- added R5: 75, Resistor_SMD:R_0805_2012Metric_Pad1.15x1.40mm_HandSolder, F.Cu at (91.7, 167.7)
- added R5: 75, Resistor_SMD:R_0805_2012Metric_Pad1.15x1.40mm_HandSolder, F.Cu at (91.7, 92.7)
- added R5: 75, Resistor_SMD:R_0805_2012Metric_Pad1.15x1.40mm_HandSolder, F.Cu at (37.7, 92.7)
- added R6: 1k402, Resistor_SMD:R_0805_2012Metric_Pad1.15x1.40mm_HandSolder, F.Cu at (56.5, 135.0)
- added R6: 1k402, Resistor_SMD:R_0805_2012Metric_Pad1.15x1.40mm_HandSolder, F.Cu at (110.5, 135.0)
- added R6: 1k402, Resistor_SMD:R_0805_2012Metric_Pad1.15x1.40mm_HandSolder, F.Cu at (110.5, 60.0)
- added R6: 1k402, Resistor_SMD:R_0805_2012Metric_Pad1.15x1.40mm_HandSolder, F.Cu at (56.5, 60.0)
- added R7: 1k402, Resistor_SMD:R_0805_2012Metric_Pad1.15x1.40mm_HandSolder, F.Cu at (108.5, 135.0)
- added R7: 1k402, Resistor_SMD:R_0805_2012Metric_Pad1.15x1.40mm_HandSolder, F.Cu at (54.5, 135.0)
- added R7: 1k402, Resistor_SMD:R_0805_2012Metric_Pad1.15x1.40mm_HandSolder, F.Cu at (108.5, 60.0)
- added R7: 1k402, Resistor_SMD:R_0805_2012Metric_Pad1.15x1.40mm_HandSolder, F.Cu at (54.5, 60.0)
- added R8: 510, Resistor_SMD:R_0805_2012Metric_Pad1.15x1.40mm_HandSolder, F.Cu at (54.8, 154.0)
- added R8: 510, Resistor_SMD:R_0805_2012Metric_Pad1.15x1.40mm_HandSolder, F.Cu at (108.8, 154.0)
- added R8: 510, Resistor_SMD:R_0805_2012Metric_Pad1.15x1.40mm_HandSolder, F.Cu at (108.8, 79.0)
- added R8: 510, Resistor_SMD:R_0805_2012Metric_Pad1.15x1.40mm_HandSolder, F.Cu at (54.8, 79.0)
- added R9: 75, Resistor_SMD:R_0805_2012Metric_Pad1.15x1.40mm_HandSolder, F.Cu at (111.8, 129.0)
- added R9: 75, Resistor_SMD:R_0805_2012Metric_Pad1.15x1.40mm_HandSolder, F.Cu at (57.8, 129.0)
- added R9: 75, Resistor_SMD:R_0805_2012Metric_Pad1.15x1.40mm_HandSolder, F.Cu at (111.8, 54.0)
- added R9: 75, Resistor_SMD:R_0805_2012Metric_Pad1.15x1.40mm_HandSolder, F.Cu at (57.8, 54.0)
- added U1: SC6206B-65K5, Package_TO_SOT_SMD:SOT-23, F.Cu at (42.6, 119.1)
- added U1: SC6206B-65K5, Package_TO_SOT_SMD:SOT-23, F.Cu at (96.6, 119.1)
- added U1: SC6206B-65K5, Package_TO_SOT_SMD:SOT-23, F.Cu at (96.6, 44.1)
- added U1: SC6206B-65K5, Package_TO_SOT_SMD:SOT-23, F.Cu at (42.6, 44.1)
- added U101: TPF144-VR, Package_SO:MSOP-10_3x3mm_P0.5mm, F.Cu at (43.5, 151.6)
- added U101: TPF144-VR, Package_SO:MSOP-10_3x3mm_P0.5mm, F.Cu at (97.5, 151.6)
- added U101: TPF144-VR, Package_SO:MSOP-10_3x3mm_P0.5mm, F.Cu at (97.5, 76.6)
- added U101: TPF144-VR, Package_SO:MSOP-10_3x3mm_P0.5mm, F.Cu at (43.5, 76.6)
- added U2: TPF144-VR, Package_SO:MSOP-10_3x3mm_P0.5mm, F.Cu at (98.8, 163.0)
- added U2: TPF144-VR, Package_SO:MSOP-10_3x3mm_P0.5mm, F.Cu at (44.8, 163.0)
- added U2: TPF144-VR, Package_SO:MSOP-10_3x3mm_P0.5mm, F.Cu at (98.8, 88.0)
- added U2: TPF144-VR, Package_SO:MSOP-10_3x3mm_P0.5mm, F.Cu at (44.8, 88.0)
- added U3: RS8752XK, Package_SO:SOIC-8_3.9x4.9mm_P1.27mm, F.Cu at (53.0, 140.9)
- added U3: RS8752XK, Package_SO:SOIC-8_3.9x4.9mm_P1.27mm, F.Cu at (107.0, 140.9)
- added U3: RS8752XK, Package_SO:SOIC-8_3.9x4.9mm_P1.27mm, F.Cu at (107.0, 65.9)
- added U3: RS8752XK, Package_SO:SOIC-8_3.9x4.9mm_P1.27mm, F.Cu at (53.0, 65.9)
- added U6: 74AHCT1G86, Package_TO_SOT_SMD:SOT-23-5, F.Cu at (33.7, 130.6)
- added U6: 74AHCT1G86, Package_TO_SOT_SMD:SOT-23-5, F.Cu at (87.7, 130.6)
- added U6: 74AHCT1G86, Package_TO_SOT_SMD:SOT-23-5, F.Cu at (87.7, 55.6)
- added U6: 74AHCT1G86, Package_TO_SOT_SMD:SOT-23-5, F.Cu at (33.7, 55.6)
- added U7: 74AHCT1G86, Package_TO_SOT_SMD:SOT-23-5, F.Cu at (38.7, 130.6)
- added U7: 74AHCT1G86, Package_TO_SOT_SMD:SOT-23-5, F.Cu at (92.7, 130.6)
- added U7: 74AHCT1G86, Package_TO_SOT_SMD:SOT-23-5, F.Cu at (92.7, 55.6)
- added U7: 74AHCT1G86, Package_TO_SOT_SMD:SOT-23-5, F.Cu at (38.7, 55.6)
- added U8: LM1881, Package_SO:SOIC-8_3.9x4.9mm_P1.27mm, F.Cu at (98.9, 139.9)
- added U8: LM1881, Package_SO:SOIC-8_3.9x4.9mm_P1.27mm, F.Cu at (44.9, 139.9)
- added U8: LM1881, Package_SO:SOIC-8_3.9x4.9mm_P1.27mm, F.Cu at (98.9, 64.9)
- added U8: LM1881, Package_SO:SOIC-8_3.9x4.9mm_P1.27mm, F.Cu at (44.9, 64.9)
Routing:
- net (no net): track 1333.1 -> 2010.9 mm, vias 228 -> 324
- net VCC: track 225.3 -> 113.3 mm, vias 4 -> 2
- net Net-(J4-Pad6): track 98.4 -> 49.2 mm
- net /2R: track 87.7 -> 43.8 mm, vias 4 -> 2
- net Net-(J4-Pad2): track 87.6 -> 43.8 mm
- net /2Y: track 81.2 -> 40.6 mm
- net /HSYNC: track 66.7 -> 33.3 mm
- net /SYNC: track 65.8 -> 32.9 mm, vias 4 -> 2
- net /Blue: track 54.1 -> 27.0 mm
- net /2B: track 53.7 -> 26.8 mm, vias 4 -> 2
- net /VSYNC: track 52.5 -> 26.3 mm
- net /Red: track 30.4 -> 15.2 mm
- net /Green: track 30.1 -> 15.1 mm
- net /2Pr: track 24.7 -> 11.4 mm
- net Net-(C1-Pad1): track 26.0 -> 13.0 mm
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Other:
- board size 105 x 145 mm -> 104 x 145 mm
- board text added: "RGB to YPbPr 2021-05-10 rev 2.4 wakabavideo.com"
- board text removed: "RGB to YPbPr 2020-06-12 rev 2.3 wakabavideo.com"
